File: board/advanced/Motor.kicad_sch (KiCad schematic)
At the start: 9 parts, among them J4 RMotor, J5 LMotor, J6 FR_ESC, J7 FL_ESC, J8 RR_ESC, J9 RL_ESC, U5 DRV8835DSSR

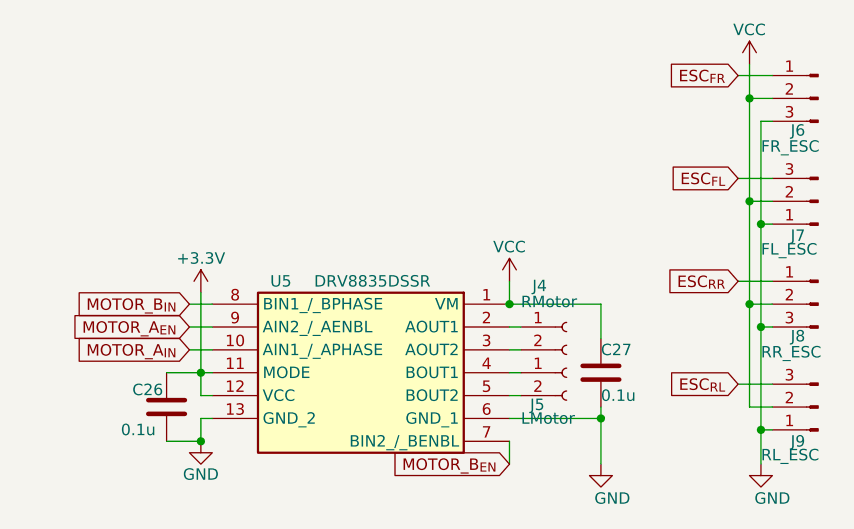
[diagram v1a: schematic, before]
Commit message: change schematics and complete wiring
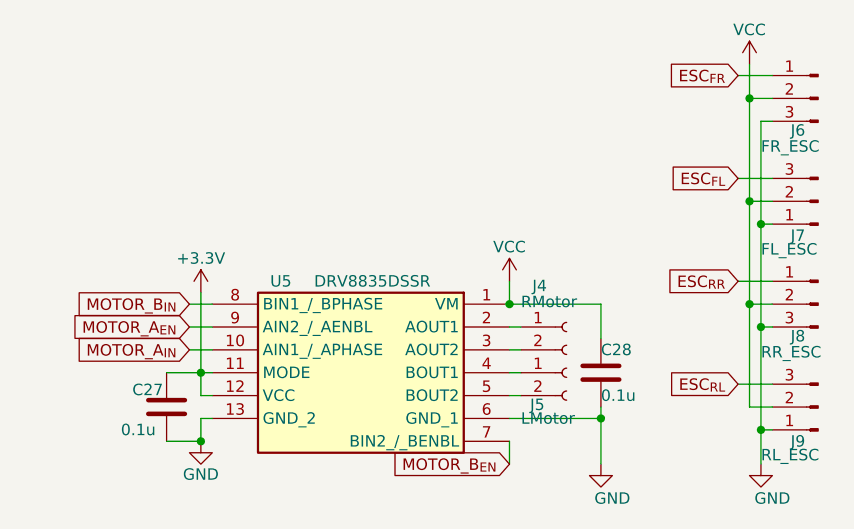
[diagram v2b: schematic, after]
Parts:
- C27: renamed from C26; footprint Capacitor_SMD:C_0201_0603Metric -> C_0402_1005Metric_small_pads:C_0402_1005Metric_small_pads
- C28: renamed from C27; footprint Capacitor_SMD:C_0201_0603Metric -> C_0402_1005Metric_small_pads:C_0402_1005Metric_small_pads
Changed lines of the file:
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@@
 		(on_board yes)
 		(dnp no)
-		(property "Reference" "#PWR040"
+		(property "Reference" "#PWR035"
 			(at 140.97 100.33 0)
 			(hide yes)
@@
 			(project "TurtlePico-Minimal"
 				(path "/7af2d99d-e350-48e7-86b4-20911ea922f3/30a58c44-3c8a-4ad6-a7be-85fee873ce7a"
-					(reference "#PWR040")
+					(reference "#PWR035")
 					(unit 1)
 				)
@@
 		(on_board yes)
 		(dnp no)
-		(property "Reference" "#PWR041"
+		(property "Reference" "#PWR036"
 			(at 151.13 123.19 0)
 			(hide yes)
@@
 			(project "TurtlePico-Minimal"
 				(path "/7af2d99d-e350-48e7-86b4-20911ea922f3/30a58c44-3c8a-4ad6-a7be-85fee873ce7a"
-					(reference "#PWR041")
+					(reference "#PWR036")
 					(unit 1)
 				)
@@
 		(on_board yes)
 		(dnp no)
-		(property "Reference" "#PWR039"
+		(property "Reference" "#PWR034"
 			(at 106.68 120.65 0)
 			(hide yes)
@@
 			(project "TurtlePico-Minimal"
 				(path "/7af2d99d-e350-48e7-86b4-20911ea922f3/30a58c44-3c8a-4ad6-a7be-85fee873ce7a"
-					(reference "#PWR039")
+					(reference "#PWR034")
 					(unit 1)
 				)
@@
 		(on_board yes)
 		(dnp no)
-		(property "Reference" "#PWR038"
+		(property "Reference" "#PWR033"
 			(at 106.68 101.6 0)
 			(hide yes)
@@
 			(project "TurtlePico-Minimal"
 				(path "/7af2d99d-e350-48e7-86b4-20911ea922f3/30a58c44-3c8a-4ad6-a7be-85fee873ce7a"
-					(reference "#PWR038")
+					(reference "#PWR033")
 					(unit 1)
 				)
@@
 		(on_board yes)
 		(dnp no)
-		(property "Reference" "C27"
+		(property "Reference" "C28"
 			(at 151.13 104.14 0)
 			(effects
@@
 			)
 		)
-		(property "Footprint" "Capacitor_SMD:C_0201_0603Metric"
+		(property "Footprint" "C_0402_1005Metric_small_pads:C_0402_1005Metric_small_pads"
 			(at 152.0952 110.49 0)
 			(hide yes)
@@
 			(project "TurtlePico-Minimal"
 				(path "/7af2d99d-e350-48e7-86b4-20911ea922f3/30a58c44-3c8a-4ad6-a7be-85fee873ce7a"
-					(reference "C27")
+					(reference "C28")
 					(unit 1)
 				)
@@
 		(on_board yes)
 		(dnp no)
-		(property "Reference" "C26"
+		(property "Reference" "C27"
 			(at 99.06 108.585 0)
 			(effects
@@
 			)
 		)
-		(property "Footprint" "Capacitor_SMD:C_0201_0603Metric"
+		(property "Footprint" "C_0402_1005Metric_small_pads:C_0402_1005Metric_small_pads"
 			(at 103.8352 114.3 0)
 			(hide yes)
@@
 			(project "TurtlePico-Minimal"
 				(path "/7af2d99d-e350-48e7-86b4-20911ea922f3/30a58c44-3c8a-4ad6-a7be-85fee873ce7a"
-					(reference "C26")
+					(reference "C27")
 					(unit 1)
 				)
@@
 		(on_board yes)
 		(dnp no)
-		(property "Reference" "#PWR043"
+		(property "Reference" "#PWR038"
 			(at 168.91 123.19 0)
 			(hide yes)
@@
 			(project "TurtlePico-Minimal"
 				(path "/7af2d99d-e350-48e7-86b4-20911ea922f3/30a58c44-3c8a-4ad6-a7be-85fee873ce7a"
-					(reference "#PWR043")
+					(reference "#PWR038")
 					(unit 1)
 				)
@@
 		(on_board yes)
 		(dnp no)
-		(property "Reference" "#PWR042"
+		(property "Reference" "#PWR037"
 			(at 167.64 76.2 0)
 			(hide yes)
@@
 			(project "TurtlePico-Minimal"
 				(path "/7af2d99d-e350-48e7-86b4-20911ea922f3/30a58c44-3c8a-4ad6-a7be-85fee873ce7a"
-					(reference "#PWR042")
-					(unit 1)
-				)
+					(reference "#PWR037")
+					(unit 1)
+				)

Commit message: add LTB example and more
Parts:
- C27: Mouser Part Number 81-GCM188R71C104KA7J -> 81-GRM15R61A104KA01J; Mouser Price/Stock https://www.mouser.jp/ProductDetail/81-GCM188R71C104KA7J -> https://www.mouser.jp/ProductDetail/Murata-Electronics/GRM1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
- C28: Mouser Part Number 81-GCM188R71C104KA7J -> 81-GRM155R71C104JA8J; Mouser Price/Stock https://www.mouser.jp/ProductDetail/81-GCM188R71C104KA7J -> https://www.mouser.jp/ProductDetail/Murata-Electronics/GRM1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
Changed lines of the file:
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@@
 			)
 		)
-		(property "Datasheet" "https://www.mouser.jp/datasheet/2/281/1/GCM188R71C104KA37_01A-3144197.pdf"
+		(property "Datasheet" ""
 			(at 151.13 106.68 0)
 			(hide yes)
@@
 			)
 		)
-		(property "Mouser Part Number" "81-GCM188R71C104KA7J"
+		(property "Mouser Part Number" "81-GRM155R71C104JA8J"
 			(at 151.13 106.68 90)
 			(hide yes)
@@
 			)
 		)
-		(property "Mouser Price/Stock" "https://www.mouser.jp/ProductDetail/81-GCM188R71C104KA7J"
+		(property "Mouser Price/Stock" "https://www.mouser.jp/ProductDetail/Murata-Electronics/GRM155R71C104JA88J?qs=hNud%2FORuBR1FShEh%252B0yzMw%3D%3D"
 			(at 151.13 106.68 90)
 			(hide yes)
@@
 			)
 		)
-		(property "Datasheet" "https://www.mouser.jp/datasheet/2/281/1/GCM188R71C104KA37_01A-3144197.pdf"
+		(property "Datasheet" ""
 			(at 102.87 110.49 0)
 			(hide yes)
@@
 			)
 		)
-		(property "Mouser Part Number" "81-GCM188R71C104KA7J"
+		(property "Mouser Part Number" "81-GRM15R61A104KA01J"
 			(at 102.87 110.49 0)
 			(hide yes)
@@
 			)
 		)
-		(property "Mouser Price/Stock" "https://www.mouser.jp/ProductDetail/81-GCM188R71C104KA7J"
+		(property "Mouser Price/Stock" "https://www.mouser.jp/ProductDetail/Murata-Electronics/GRM155R61A104KA01J?qs=sGAEpiMZZMsh%252B1woXyUXj4f5sDJ%252BKZJJAX4rsnlerMM%3D"
 			(at 102.87 110.49 0)
 			(hide yes)
